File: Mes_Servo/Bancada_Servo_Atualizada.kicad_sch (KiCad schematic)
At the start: 11 parts, among them M1 Motor_Servo, U1 INA219, U3 AS5600, U4 ESP32-DEVKIT-V1

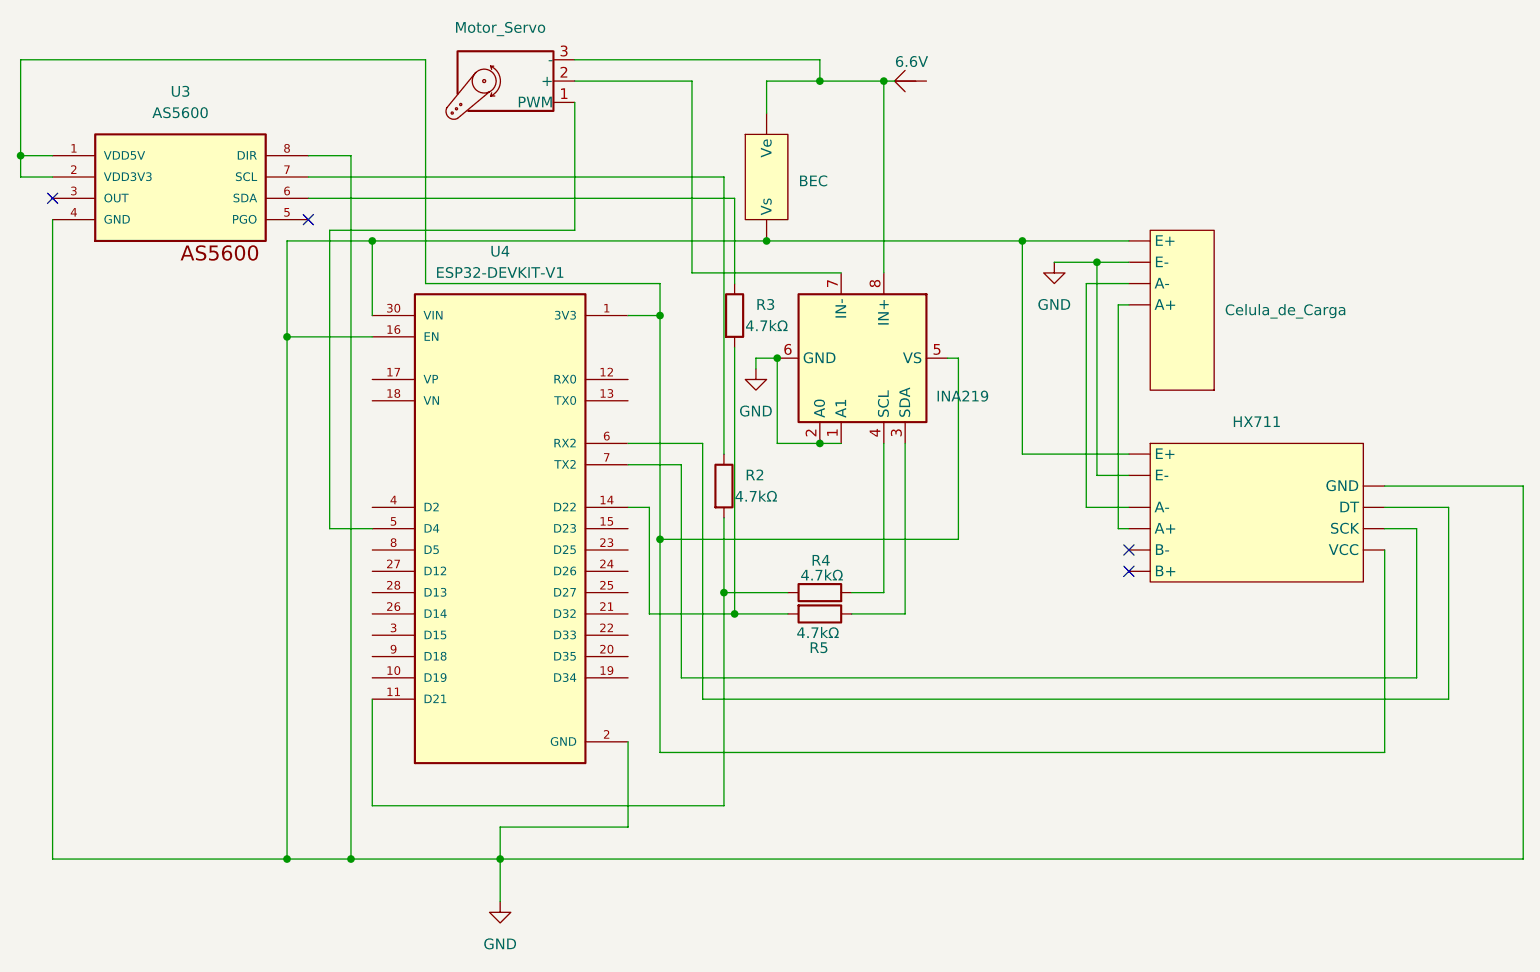
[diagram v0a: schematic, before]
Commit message: V3 Esquemático Kicad Bancada do servo
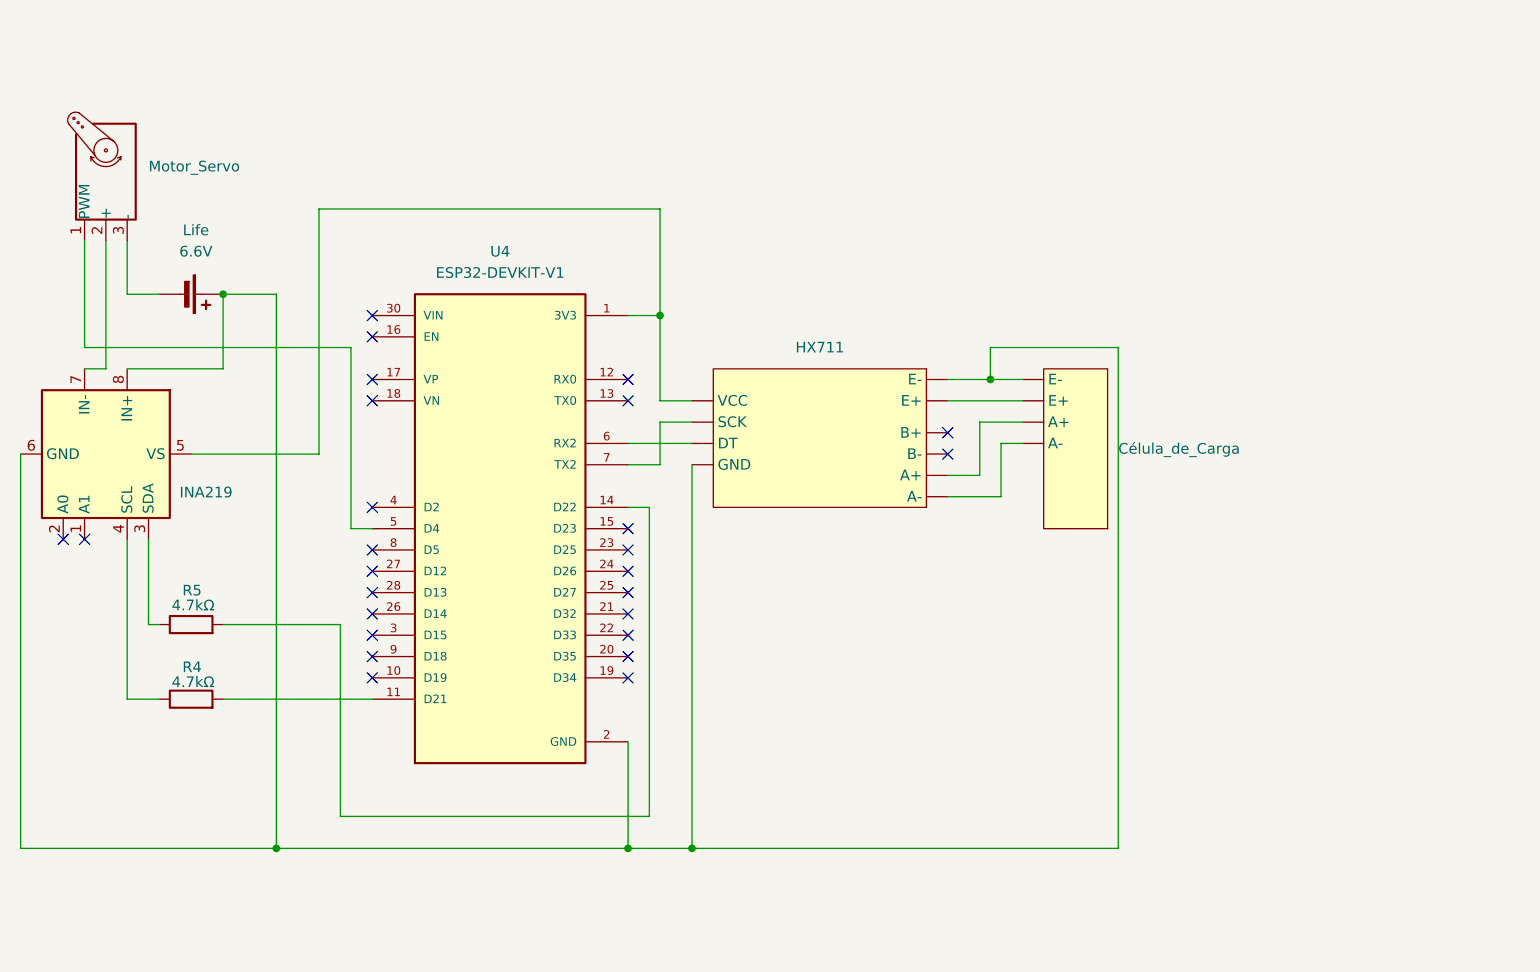
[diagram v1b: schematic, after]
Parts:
- removed BEC: (no value), symbol Servos:BEC
- removed Celula_de_Carga: (no value), symbol Servos:Celula_de_Carga
- removed R2, R3: 4.7kΩ, symbol Device:R
- removed U3: AS5600, AS5600:SOIC8, symbol Servos:AS5600
- added Célula_de_Carga: (no value), symbol Servos:Celula_de_Carga
- added Life: 6.6V, symbol Device:Battery_Cell
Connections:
- net GND: now also U1.8 (IN+), Célula_de_Carga. (E-), Life.1 (+); no longer U1.1 (A1), U1.2 (A0), U4.16 (EN), U4.30 (VIN)
- net at U1.4 (SCL): now also R4.1; no longer R4.2
- net at M1.3 (-): now also Life.2 (-); no longer U1.8 (IN+)
- net at U4.11 (D21): now also R4.2; no longer R4.1
- new net: Célula_de_Carga. (E-), HX711. (VCC) (x3)
- no-connect marks 4 -> 26
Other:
- moved on the sheet: R4, R5
